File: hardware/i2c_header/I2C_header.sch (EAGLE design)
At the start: 6 parts, among them X6 I2C

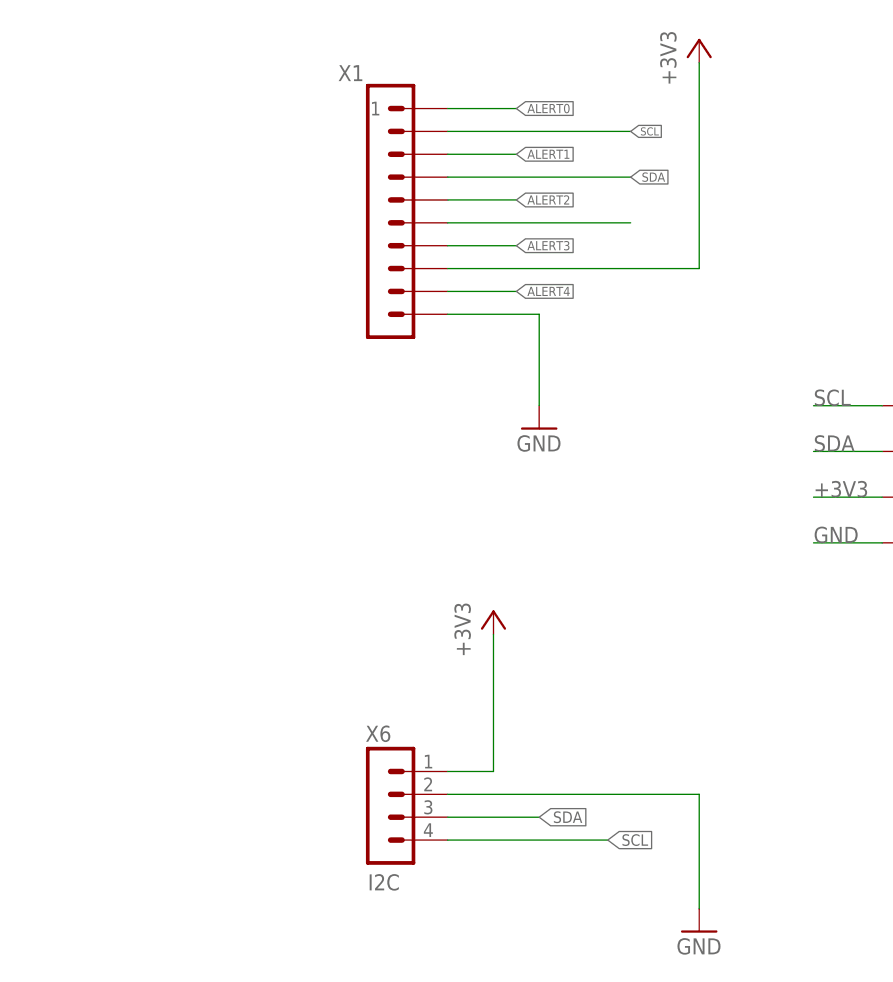
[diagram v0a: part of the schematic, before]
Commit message: header pinout changed
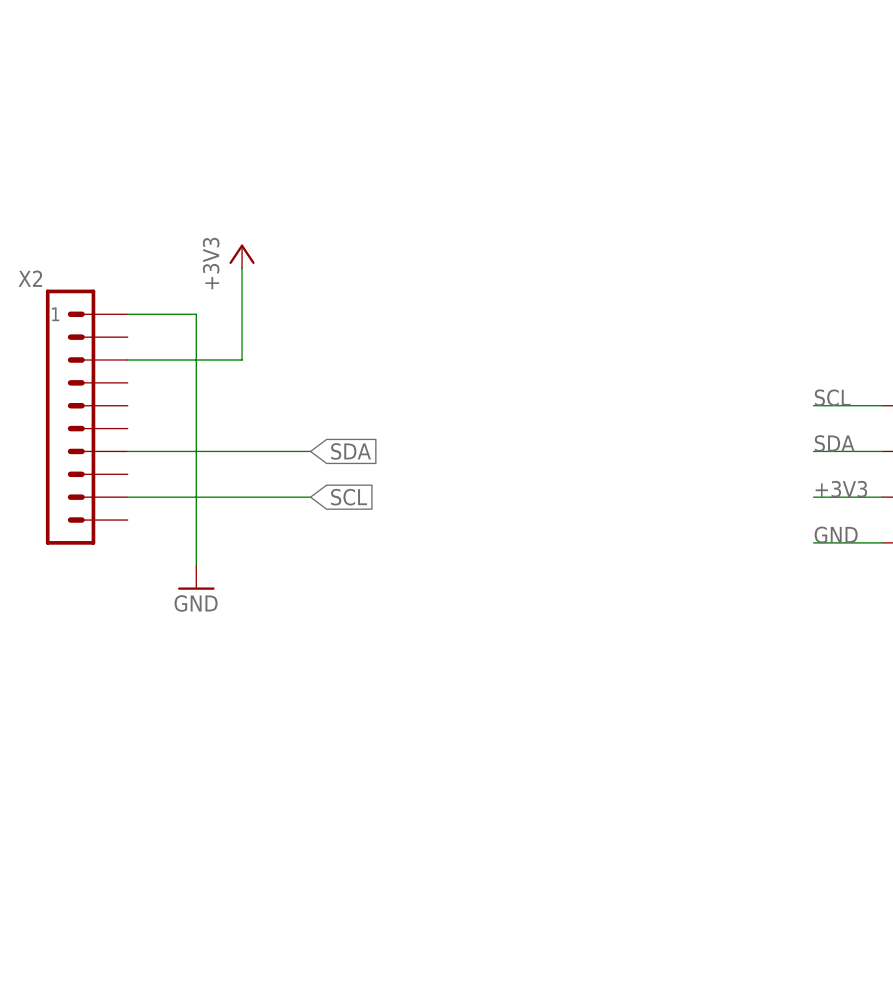
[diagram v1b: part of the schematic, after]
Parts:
- removed X1: (no value), SIG_Parts:FFC_10PLARGE
- removed X6: I2C, RAK3172_board:JST04_PH
- added X2: (no value), SIG_Parts:FFC_10PLARGE
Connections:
- removed net ALERT0: X1G$1.1
- removed net ALERT1: X1G$1.3
- removed net ALERT2: X1G$1.5
- removed net ALERT3: X1G$1.7
- removed net ALERT4: X1G$1.9
- removed net N$6: X1G$1.6
- net +3V3: now also X2G$1.3; no longer X1G$1.8, X6.1
- net GND: now also X2G$1.1; no longer X1G$1.10, X6.2
- net SCL: now also X2G$1.9; no longer X1G$1.2, X6.4
- net SDA: now also X2G$1.7; no longer X1G$1.4, X6.3
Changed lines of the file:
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@@
 </classes>
 <parts>
-<part name="GND9" library="temp_sens_ring" library_urn="urn:adsk.eagle:library:31797301" deviceset="GND" device=""/>
-<part name="+3V8" library="temp_sens_ring" library_urn="urn:adsk.eagle:library:31797301" deviceset="+3V3" device=""/>
-<part name="X1" library="SIG_Parts" deviceset="FFC_10P" device="LARGE"/>
-<part name="X6" library="RAK3172_board" library_urn="urn:adsk.eagle:library:32884481" deviceset="JST04_*" device="PH" package3d_urn="urn:adsk.eagle:package:32884558/2" value="I2C"/>
-<part name="+3V1" library="temp_sens_ring" library_urn="urn:adsk.eagle:library:31797301" deviceset="+3V3" device=""/>
-<part name="GND1" library="temp_sens_ring" library_urn="urn:adsk.eagle:library:31797301" deviceset="GND" device=""/>
 <part name="U$1" library="SIG_Parts" deviceset="PAD3.0X5.0" device=""/>
 <part name="U$2" library="SIG_Parts" deviceset="PAD3.0X5.0" device=""/>
 <part name="U$3" library="SIG_Parts" deviceset="PAD3.0X5.0" device=""/>
 <part name="U$4" library="SIG_Parts" deviceset="PAD3.0X5.0" device=""/>
+<part name="X2" library="SIG_Parts" deviceset="FFC_10P" device="LARGE"/>
+<part name="GND2" library="temp_sens_ring" library_urn="urn:adsk.eagle:library:31797301" deviceset="GND" device=""/>
+<part name="+3V2" library="temp_sens_ring" library_urn="urn:adsk.eagle:library:31797301" deviceset="+3V3" device=""/>
 </parts>
 <sheets>
@@
 </plain>
 <instances>
-<instance part="GND9" gate="1" x="40.64" y="38.1" smashed="yes">
-<attribute name="VALUE" x="38.1" y="35.56" size="1.778" layer="96"/>
-</instance>
-<instance part="+3V8" gate="G$1" x="58.42" y="81.28" smashed="yes">
-<attribute name="VALUE" x="55.88" y="76.2" size="1.778" layer="96" rot="R90"/>
-</instance>
-<instance part="X1" gate="G$1" x="22.86" y="63.5" smashed="yes">
-<attribute name="VALUE" x="17.526" y="45.72" size="1.778" layer="96"/>
-<attribute name="NAME" x="18.288" y="76.708" size="1.778" layer="95"/>
-</instance>
-<instance part="X6" gate="G$1" x="22.86" y="-5.08" smashed="yes" rot="MR180">
-<attribute name="VALUE" x="21.59" y="-11.43" size="1.778" layer="96" rot="MR180"/>
-<attribute name="NAME" x="21.336" y="5.08" size="1.778" layer="95" rot="MR180"/>
-</instance>
-<instance part="+3V1" gate="G$1" x="35.56" y="17.78" smashed="yes">
-<attribute name="VALUE" x="33.02" y="12.7" size="1.778" layer="96" rot="R90"/>
-</instance>
-<instance part="GND1" gate="1" x="58.42" y="-17.78" smashed="yes">
-<attribute name="VALUE" x="55.88" y="-20.32" size="1.778" layer="96"/>
-</instance>
 <instance part="U$1" gate="G$1" x="83.82" y="40.64" smashed="yes">
 <attribute name="NAME" x="86.868" y="39.878" size="1.778" layer="95"/>
@@
 <attribute name="NAME" x="86.868" y="24.638" size="1.778" layer="95"/>
 </instance>
+<instance part="X2" gate="G$1" x="-12.7" y="40.64" smashed="yes">
+<attribute name="VALUE" x="-18.034" y="22.86" size="1.778" layer="96"/>
+<attribute name="NAME" x="-17.272" y="53.848" size="1.778" layer="95"/>
+</instance>
+<instance part="GND2" gate="1" x="2.54" y="20.32" smashed="yes">
+<attribute name="VALUE" x="0" y="17.78" size="1.778" layer="96"/>
+</instance>
+<instance part="+3V2" gate="G$1" x="7.62" y="58.42" smashed="yes">
+<attribute name="VALUE" x="5.08" y="53.34" size="1.778" layer="96" rot="R90"/>
+</instance>
 </instances>
 <busses>
@@
 <net name="GND" class="0">
 <segment>
-<wire x1="30.48" y1="50.8" x2="40.64" y2="50.8" width="0.1524" layer="91"/>
-<wire x1="40.64" y1="50.8" x2="40.64" y2="40.64" width="0.1524" layer="91"/>
-<pinref part="GND9" gate="1" pin="GND"/>
-<pinref part="X1" gate="G$1" pin="10"/>
-</segment>
-<segment>
-<pinref part="X6" gate="G$1" pin="2"/>
-<wire x1="30.48" y1="-2.54" x2="58.42" y2="-2.54" width="0.1524" layer="91"/>
-<wire x1="58.42" y1="-2.54" x2="58.42" y2="-15.24" width="0.1524" layer="91"/>
-<pinref part="GND1" gate="1" pin="GND"/>
-</segment>
-<segment>
 <pinref part="U$4" gate="G$1" pin="P$1"/>
 <wire x1="78.74" y1="25.4" x2="71.12" y2="25.4" width="0.1524" layer="91"/>
 <label x="71.12" y="25.4" size="1.778" layer="95"/>
 </segment>
+<segment>
+<pinref part="X2" gate="G$1" pin="1"/>
+<wire x1="-5.08" y1="50.8" x2="2.54" y2="50.8" width="0.1524" layer="91"/>
+<wire x1="2.54" y1="50.8" x2="2.54" y2="22.86" width="0.1524" layer="91"/>
+<pinref part="GND2" gate="1" pin="GND"/>
+</segment>
 </net>
 <net name="+3V3" class="0">
-<segment>
-<wire x1="30.48" y1="55.88" x2="58.42" y2="55.88" width="0.1524" layer="91"/>
-<wire x1="58.42" y1="55.88" x2="58.42" y2="78.74" width="0.1524" layer="91"/>
-<pinref part="+3V8" gate="G$1" pin="+3V3"/>
-<pinref part="X1" gate="G$1" pin="8"/>
-</segment>
-<segment>
-<pinref part="X6" gate="G$1" pin="1"/>
-<wire x1="30.48" y1="0" x2="35.56" y2="0" width="0.1524" layer="91"/>
-<wire x1="35.56" y1="0" x2="35.56" y2="15.24" width="0.1524" layer="91"/>
-<pinref part="+3V1" gate="G$1" pin="+3V3"/>
-</segment>
 <segment>
 <pinref part="U$3" gate="G$1" pin="P$1"/>
@@
 <label x="71.12" y="30.48" size="1.778" layer="95"/>
 </segment>
+<segment>
+<pinref part="X2" gate="G$1" pin="3"/>
+<wire x1="-5.08" y1="45.72" x2="7.62" y2="45.72" width="0.1524" layer="91"/>
+<wire x1="7.62" y1="45.72" x2="7.62" y2="55.88" width="0.1524" layer="91"/>
+<pinref part="+3V2" gate="G$1" pin="+3V3"/>
+</segment>
 </net>
 <net name="SDA" class="0">
-<segment>
-<wire x1="30.48" y1="66.04" x2="50.8" y2="66.04" width="0.1524" layer="91"/>
-<label x="50.8" y="66.04" size="1.016" layer="95" xref="yes"/>
-<pinref part="X1" gate="G$1" pin="4"/>
-</segment>
-<segment>
-<pinref part="X6" gate="G$1" pin="3"/>
-<wire x1="30.48" y1="-5.08" x2="40.64" y2="-5.08" width="0.1524" layer="91"/>
-<label x="40.64" y="-5.08" size="1.27" layer="95" rot="MR180" xref="yes"/>
-</segment>
 <segment>
 <pinref part="U$2" gate="G$1" pin="P$1"/>
@@
 <label x="71.12" y="35.56" size="1.778" layer="95"/>
 </segment>
+<segment>
+<pinref part="X2" gate="G$1" pin="7"/>
+<wire x1="-5.08" y1="35.56" x2="15.24" y2="35.56" width="0.1524" layer="91"/>
+<label x="15.24" y="35.56" size="1.778" layer="95" xref="yes"/>
+</segment>
 </net>
 <net name="SCL" class="0">
-<segment>
-<wire x1="30.48" y1="71.12" x2="50.8" y2="71.12" width="0.1524" layer="91"/>
-<label x="50.8" y="71.12" size="0.889" layer="95" xref="yes"/>
-<pinref part="X1" gate="G$1" pin="2"/>
-</segment>
-<segment>
-<pinref part="X6" gate="G$1" pin="4"/>
-<wire x1="30.48" y1="-7.62" x2="48.26" y2="-7.62" width="0.1524" layer="91"/>
-<label x="48.26" y="-7.62" size="1.27" layer="95" rot="MR180" xref="yes"/>
-</segment>
 <segment>
 <pinref part="U$1" gate="G$1" pin="P$1"/>
@@
 <label x="71.12" y="40.64" size="1.778" layer="95"/>
 </segment>
-</net>
-<net name="ALERT1" class="0">
 <segment>
-<wire x1="30.48" y1="68.58" x2="38.1" y2="68.58" width="0.1524" layer="91"/>
-<label x="38.1" y="68.58" size="1.016" layer="95" xref="yes"/>
-<pinref part="X1" gate="G$1" pin="3"/>
-</segment>
-</net>
-<net name="ALERT2" class="0">
-<segment>
-<wire x1="30.48" y1="63.5" x2="38.1" y2="63.5" width="0.1524" layer="91"/>
-<label x="38.1" y="63.5" size="1.016" layer="95" xref="yes"/>
-<pinref part="X1" gate="G$1" pin="5"/>
-</segment>
-</net>
-<net name="ALERT3" class="0">
-<segment>
-<wire x1="30.48" y1="58.42" x2="38.1" y2="58.42" width="0.1524" layer="91"/>
-<label x="38.1" y="58.42" size="1.016" layer="95" xref="yes"/>
-<pinref part="X1" gate="G$1" pin="7"/>
-</segment>
-</net>
-<net name="ALERT4" class="0">
-<segment>
-<wire x1="30.48" y1="53.34" x2="38.1" y2="53.34" width="0.1524" layer="91"/>
-<label x="38.1" y="53.34" size="1.016" layer="95" xref="yes"/>
-<pinref part="X1" gate="G$1" pin="9"/>
-</segment>
-</net>
-<net name="ALERT0" class="0">
-<segment>
-<wire x1="30.48" y1="73.66" x2="38.1" y2="73.66" width="0.1524" layer="91"/>
-<label x="38.1" y="73.66" size="1.016" layer="95" xref="yes"/>
-<pinref part="X1" gate="G$1" pin="1"/>
-</segment>
-</net>
-<net name="N$6" class="0">
-<segment>
-<wire x1="30.48" y1="60.96" x2="50.8" y2="60.96" width="0.1524" layer="91"/>
-<pinref part="X1" gate="G$1" pin="6"/>
+<pinref part="X2" gate="G$1" pin="9"/>
+<wire x1="-5.08" y1="30.48" x2="15.24" y2="30.48" width="0.1524" layer="91"/>
+<label x="15.24" y="30.48" size="1.778" layer="95" xref="yes"/>
 </segment>
 </net>
@@
 will not be understood (or retained) with this version.
 </note>
-<note version="8.3" severity="warning">
-Since Version 8.3, EAGLE supports the association of 3D packages
-with devices in libraries, schematics, and board files. Those 3D
-packages will not be understood (or retained) with this version.
-</note>
 </compatibility>

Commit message: Latest hardware designs
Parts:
- added Q1: BSS84, SIG_Parts:BSS84
- added Q2: BSS138, SIG_Parts:BSS138
- added R1, R2: (no value), SIG_Parts:RESISTOR_0805
- added U$5: PAD3.0X5.0, SIG_Parts:PAD3.0X5.0
- added X1: 22-23-2021, con-molex:22-23-2021
- X2: value (none) -> 22-23-2021; device SIG_Parts:FFC_10PLARGE -> con-molex:22-23-2021
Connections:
- new net N$1: Q1.D, X2-2.S
- new net N$2: Q1.G, Q2.D, R1.2
- new net PWR_ON: Q2.G, R2.2, U$5.P$1
- net +3V3: now also Q1.S, R1.1; no longer X2G$1.3
- net GND: now also Q2.S, R2.1, X2-1.S; no longer X2G$1.1
- net SCL: now also X1-2.S; no longer X2G$1.9
- net SDA: now also X1-1.S; no longer X2G$1.7
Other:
- moved on the sheet: U$1, U$2, U$3, U$4
